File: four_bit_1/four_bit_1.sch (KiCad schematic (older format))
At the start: 1 part, among them P1 DIN_41612_128P

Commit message: Added in WHOMP, whatever it is
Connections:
- net CI05/: now also P1.67 (3C); no longer P1.65 (1C)
- net CO06: now also P1.68 (4C); no longer P1.66 (2C)
- net G01/: now also P1.69 (5C); no longer P1.67 (3C)
- net GND: no longer P1.77 (13C), P1.78 (14C)
- net L01/: now also P1.70 (6C); no longer P1.68 (4C)
- net L02/: now also P1.71 (7C); no longer P1.69 (5C)
- net L04/: now also P1.72 (8C); no longer P1.70 (6C)
- net WL01/: now also P1.73 (9C); no longer P1.71 (7C)
- net WL02/: now also P1.74 (10C); no longer P1.72 (8C)
- net WL03/: now also P1.75 (11C); no longer P1.73 (9C)
- net WL04/: now also P1.76 (12C); no longer P1.74 (10C)
- net XUY01/: now also P1.77 (13C); no longer P1.75 (11C)
- net XUY02/: now also P1.78 (14C); no longer P1.76 (12C)
- new net WHOMP: P1.65 (1C)
- new net WHOMPA: P1.66 (2C)
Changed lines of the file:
@@
 $EndDescr
 $Sheet
-S 1750 1200 1400 7250
+S 1750 1200 1400 7600
 U 5684C508
 F0 "A08_1" 60
@@
 F60 "_WL1" O R 3150 4050 60
 F61 "_WL1/" O R 3150 4150 60
-F62 "_MWL1" O R 3150 4600 60
+F62 "_MWL1" O R 3150 4750 60
 F63 "_CI_OUT" O R 3150 2750 60
 F64 "_CO_IN" I L 1750 3650 60
@@
 F96 "_WL2" O R 3150 4250 60
 F97 "_WL2/" O R 3150 4350 60
-F98 "_MWL2" O R 3150 4700 60
+F98 "_MWL2" O R 3150 4850 60
 F99 "_RL1/" O R 3150 3850 60
 F100 "_RL2/" O R 3150 3950 60
+F101 "_RL_OUT_2" O R 3150 4600 60
+F102 "_RL_OUT_1" O R 3150 4500 60
+F103 "_WHOMPA" I L 1750 8700 60
+F104 "_WHOMP_1" I L 1750 8500 60
+F105 "_WHOMP_2" I L 1750 8600 60
 $EndSheet
 $Comp
@@
 $EndComp
 $Sheet
-S 4300 1200 1400 7250
+S 4300 1200 1400 7600
 U 5689EF80
 F0 "A08_2" 60
@@
 F60 "_WL1" O R 5700 4050 60
 F61 "_WL1/" O R 5700 4150 60
-F62 "_MWL1" O R 5700 4600 60
+F62 "_MWL1" O R 5700 4750 60
 F63 "_CI_OUT" O R 5700 2750 60
 F64 "_CO_IN" I L 4300 3650 60
@@
 F96 "_WL2" O R 5700 4250 60
 F97 "_WL2/" O R 5700 4350 60
-F98 "_MWL2" O R 5700 4700 60
+F98 "_MWL2" O R 5700 4850 60
 F99 "_RL1/" O R 5700 3850 60
 F100 "_RL2/" O R 5700 3950 60
+F101 "_RL_OUT_2" O R 5700 4600 60
+F102 "_RL_OUT_1" O R 5700 4500 60
+F103 "_WHOMPA" I L 4300 8700 60
+F104 "_WHOMP_1" I L 4300 8500 60
+F105 "_WHOMP_2" I L 4300 8600 60
 $EndSheet
 Text GLabel 1650 1300 0    60   Input ~ 0
@@
 $EndComp
 Wire Wire Line
-	9700 2150 9800 2150
-Wire Wire Line
-	9700 2250 9800 2250
-Connection ~ 9700 2250
-Wire Wire Line
 	9700 2350 9800 2350
-Connection ~ 9700 2350
 Wire Wire Line
 	9700 2450 9800 2450
@@
 Text Label 5850 2000 0    60   ~ 0
 G04/
-Text GLabel 9700 1250 0    60   Input ~ 0
+Text GLabel 9700 1450 0    60   Input ~ 0
 L01/
 Wire Wire Line
-	9800 1250 9700 1250
-Text GLabel 9700 1350 0    60   Input ~ 0
+	9800 1450 9700 1450
+Text GLabel 9700 1550 0    60   Input ~ 0
 L02/
 Wire Wire Line
-	9800 1350 9700 1350
-Wire Wire Line
-	9700 2150 9700 4200
-Text GLabel 9700 1550 0    60   BiDi ~ 0
+	9800 1550 9700 1550
+Wire Wire Line
+	9700 2350 9700 4200
+Text GLabel 9700 1750 0    60   BiDi ~ 0
 WL01/
-Wire Wire Line
-	9800 1550 9700 1550
-Text GLabel 9700 1650 0    60   BiDi ~ 0
-WL02/
-Wire Wire Line
-	9800 1650 9700 1650
-Text GLabel 9700 1750 0    60   BiDi ~ 0
-WL03/
 Wire Wire Line
 	9800 1750 9700 1750
 Text GLabel 9700 1850 0    60   BiDi ~ 0
+WL02/
+Wire Wire Line
+	9800 1850 9700 1850
+Text GLabel 9700 1950 0    60   BiDi ~ 0
+WL03/
+Wire Wire Line
+	9800 1950 9700 1950
+Text GLabel 9700 2050 0    60   BiDi ~ 0
 WL04/
 Wire Wire Line
-	9800 1850 9700 1850
+	9800 2050 9700 2050
 Text GLabel 5800 2750 2    60   Output ~ 0
 CI05/
@@
 Wire Wire Line
 	5700 2850 5800 2850
-Text GLabel 9700 950  0    60   Input ~ 0
+Text GLabel 9700 1150 0    60   Input ~ 0
 CI05/
 Wire Wire Line
-	9800 950  9700 950
-Text GLabel 9700 1050 0    60   Input ~ 0
+	9800 1150 9700 1150
+Text GLabel 9700 1250 0    60   Input ~ 0
 CO06
 Wire Wire Line
-	9800 1050 9700 1050
+	9800 1250 9700 1250
 Text GLabel 5800 2200 2    60   Output ~ 0
 L04/
 Wire Wire Line
 	5700 2200 5800 2200
-Text GLabel 9700 1450 0    60   Input ~ 0
+Text GLabel 9700 1650 0    60   Input ~ 0
 L04/
 Wire Wire Line
-	9800 1450 9700 1450
+	9800 1650 9700 1650
 Wire Wire Line
 	3150 1800 3250 1800
 Text GLabel 3250 1800 2    60   Output ~ 0
 G01/
-Text GLabel 9700 1150 0    60   Input ~ 0
+Text GLabel 9700 1350 0    60   Input ~ 0
 G01/
 Wire Wire Line
-	9800 1150 9700 1150
+	9800 1350 9700 1350
 Text GLabel 3250 3350 2    60   Output ~ 0
 XUY01/
@@
 Wire Wire Line
 	3150 3450 3250 3450
-Text GLabel 9700 1950 0    60   Input ~ 0
+Text GLabel 9700 2150 0    60   Input ~ 0
 XUY01/
 Wire Wire Line
-	9800 1950 9700 1950
-Text GLabel 9700 2050 0    60   Input ~ 0
+	9800 2150 9700 2150
+Text GLabel 9700 2250 0    60   Input ~ 0
 XUY02/
 Wire Wire Line
-	9800 2050 9700 2050
+	9800 2250 9700 2250
+Text GLabel 1650 8700 0    60   Input ~ 0
+WHOMPA
+Wire Wire Line
+	1750 8700 1650 8700
+$Comp
+L GND #PWR09
+U 1 1 56BB3258
+P 3750 8800
+F 0 "#PWR09" H 3750 8550 50  0001 C CNN
+F 1 "GND" H 3750 8650 50  0000 C CNN
+F 2 "" H 3750 8800 60  0000 C CNN
+F 3 "" H 3750 8800 60  0000 C CNN
+	1    3750 8800
+	1    0    0    -1
+$EndComp
+Wire Wire Line
+	4300 8700 3750 8700
+Text GLabel 1650 8600 0    60   Input ~ 0
+WHOMP
+Wire Wire Line
+	1750 8600 1650 8600
+$Comp
+L GND #PWR010
+U 1 1 56C05747
+P 1050 8600
+F 0 "#PWR010" H 1050 8350 50  0001 C CNN
+F 1 "GND" H 1050 8450 50  0000 C CNN
+F 2 "" H 1050 8600 60  0000 C CNN
+F 3 "" H 1050 8600 60  0000 C CNN
+	1    1050 8600
+	1    0    0    -1
+$EndComp
+Wire Wire Line
+	1750 8500 1050 8500
+Wire Wire Line
+	1050 8500 1050 8600
+Connection ~ 3750 8700
+Text GLabel 4200 8600 0    60   Input ~ 0
+WHOMP
+Wire Wire Line
+	4300 8600 4200 8600
+Wire Wire Line
+	3750 8500 3750 8800
+Wire Wire Line
+	3750 8500 4300 8500
+Text GLabel 9700 950  0    60   Output ~ 0
+WHOMP
+Wire Wire Line
+	9800 950  9700 950
+Text GLabel 9700 1050 0    60   Output ~ 0
+WHOMPA
+Wire Wire Line
+	9800 1050 9700 1050
 $EndSCHEMATC

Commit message: Added and tied in module 12, parity & s register
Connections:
- net G01/: now also P1.70 (6C); no longer P1.69 (5C)
- net GND: no longer P1.79 (15C), P1.80 (16C), P1.81 (17C), P1.82 (18C)
- net L01/: now also P1.74 (10C); no longer P1.70 (6C)
- net L02/: now also P1.75 (11C); no longer P1.71 (7C)
- net L04/: now also P1.76 (12C); no longer P1.72 (8C)
- net WL01/: now also P1.77 (13C); no longer P1.73 (9C)
- net WL02/: now also P1.78 (14C); no longer P1.74 (10C)
- net WL03/: now also P1.79 (15C); no longer P1.75 (11C)
- net WL04/: now also P1.80 (16C); no longer P1.76 (12C)
- net XUY01/: now also P1.81 (17C); no longer P1.77 (13C)
- net XUY02/: now also P1.82 (18C); no longer P1.78 (14C)
- new net G01: P1.69 (5C)
- new net G02: P1.71 (7C)
- new net G03: P1.72 (8C)
- new net G04: P1.73 (9C)
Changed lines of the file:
@@
 $EndComp
 Wire Wire Line
-	9700 2350 9800 2350
-Wire Wire Line
-	9700 2450 9800 2450
-Connection ~ 9700 2450
-Wire Wire Line
-	9700 2550 9800 2550
-Connection ~ 9700 2550
-Wire Wire Line
-	9700 2650 9800 2650
-Connection ~ 9700 2650
-Wire Wire Line
 	9700 2750 9800 2750
-Connection ~ 9700 2750
 Wire Wire Line
 	9700 2850 9800 2850
@@
 Text Label 5850 2000 0    60   ~ 0
 G04/
-Text GLabel 9700 1450 0    60   Input ~ 0
+Text GLabel 9700 1850 0    60   Input ~ 0
 L01/
 Wire Wire Line
-	9800 1450 9700 1450
-Text GLabel 9700 1550 0    60   Input ~ 0
+	9800 1850 9700 1850
+Text GLabel 9700 1950 0    60   Input ~ 0
 L02/
 Wire Wire Line
-	9800 1550 9700 1550
-Wire Wire Line
-	9700 2350 9700 4200
-Text GLabel 9700 1750 0    60   BiDi ~ 0
+	9800 1950 9700 1950
+Text GLabel 9700 2150 0    60   BiDi ~ 0
 WL01/
 Wire Wire Line
-	9800 1750 9700 1750
-Text GLabel 9700 1850 0    60   BiDi ~ 0
+	9800 2150 9700 2150
+Text GLabel 9700 2250 0    60   BiDi ~ 0
 WL02/
 Wire Wire Line
-	9800 1850 9700 1850
-Text GLabel 9700 1950 0    60   BiDi ~ 0
+	9800 2250 9700 2250
+Text GLabel 9700 2350 0    60   BiDi ~ 0
 WL03/
 Wire Wire Line
-	9800 1950 9700 1950
-Text GLabel 9700 2050 0    60   BiDi ~ 0
+	9800 2350 9700 2350
+Text GLabel 9700 2450 0    60   BiDi ~ 0
 WL04/
 Wire Wire Line
-	9800 2050 9700 2050
+	9800 2450 9700 2450
 Text GLabel 5800 2750 2    60   Output ~ 0
 CI05/
@@
 Wire Wire Line
 	5700 2200 5800 2200
-Text GLabel 9700 1650 0    60   Input ~ 0
+Text GLabel 9700 2050 0    60   Input ~ 0
 L04/
 Wire Wire Line
-	9800 1650 9700 1650
+	9800 2050 9700 2050
 Wire Wire Line
 	3150 1800 3250 1800
 Text GLabel 3250 1800 2    60   Output ~ 0
 G01/
-Text GLabel 9700 1350 0    60   Input ~ 0
+Text GLabel 9700 1450 0    60   Input ~ 0
 G01/
 Wire Wire Line
-	9800 1350 9700 1350
+	9800 1450 9700 1450
 Text GLabel 3250 3350 2    60   Output ~ 0
 XUY01/
@@
 Wire Wire Line
 	3150 3450 3250 3450
-Text GLabel 9700 2150 0    60   Input ~ 0
+Text GLabel 9700 2550 0    60   Input ~ 0
 XUY01/
 Wire Wire Line
-	9800 2150 9700 2150
-Text GLabel 9700 2250 0    60   Input ~ 0
+	9800 2550 9700 2550
+Text GLabel 9700 2650 0    60   Input ~ 0
 XUY02/
 Wire Wire Line
-	9800 2250 9700 2250
+	9800 2650 9700 2650
 Text GLabel 1650 8700 0    60   Input ~ 0
 WHOMPA
@@
 Wire Wire Line
 	9800 1050 9700 1050
+Wire Wire Line
+	3150 1700 3250 1700
+Text GLabel 3250 1700 2    60   Output ~ 0
+G01
+Wire Wire Line
+	3150 1900 3250 1900
+Text GLabel 3250 1900 2    60   Output ~ 0
+G02
+Wire Wire Line
+	5700 1700 5800 1700
+Text GLabel 5800 1700 2    60   Output ~ 0
+G03
+Wire Wire Line
+	5700 1900 5800 1900
+Text GLabel 5800 1900 2    60   Output ~ 0
+G04
+Wire Wire Line
+	9700 2750 9700 4200
+Text GLabel 9700 1350 0    60   Input ~ 0
+G01
+Wire Wire Line
+	9800 1350 9700 1350
+Text GLabel 9700 1550 0    60   Input ~ 0
+G02
+Wire Wire Line
+	9800 1550 9700 1550
+Text GLabel 9700 1650 0    60   Input ~ 0
+G03
+Wire Wire Line
+	9800 1650 9700 1650
+Text GLabel 9700 1750 0    60   Input ~ 0
+G04
+Wire Wire Line
+	9800 1750 9700 1750
 $EndSCHEMATC

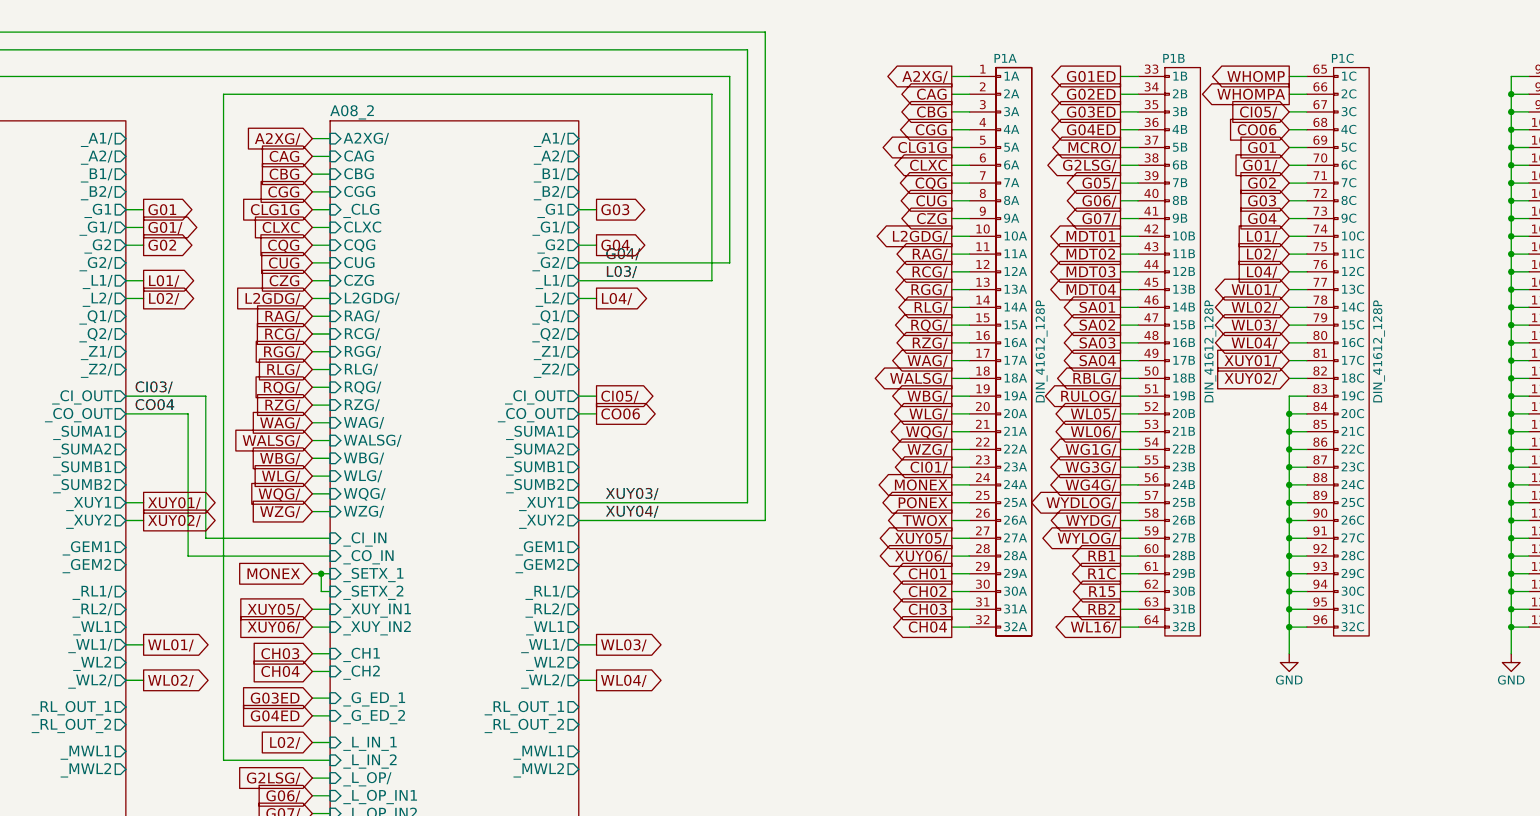
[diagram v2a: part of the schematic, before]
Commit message: Added and tied in module 15, the rupt service (and banking/rope+strand selection)
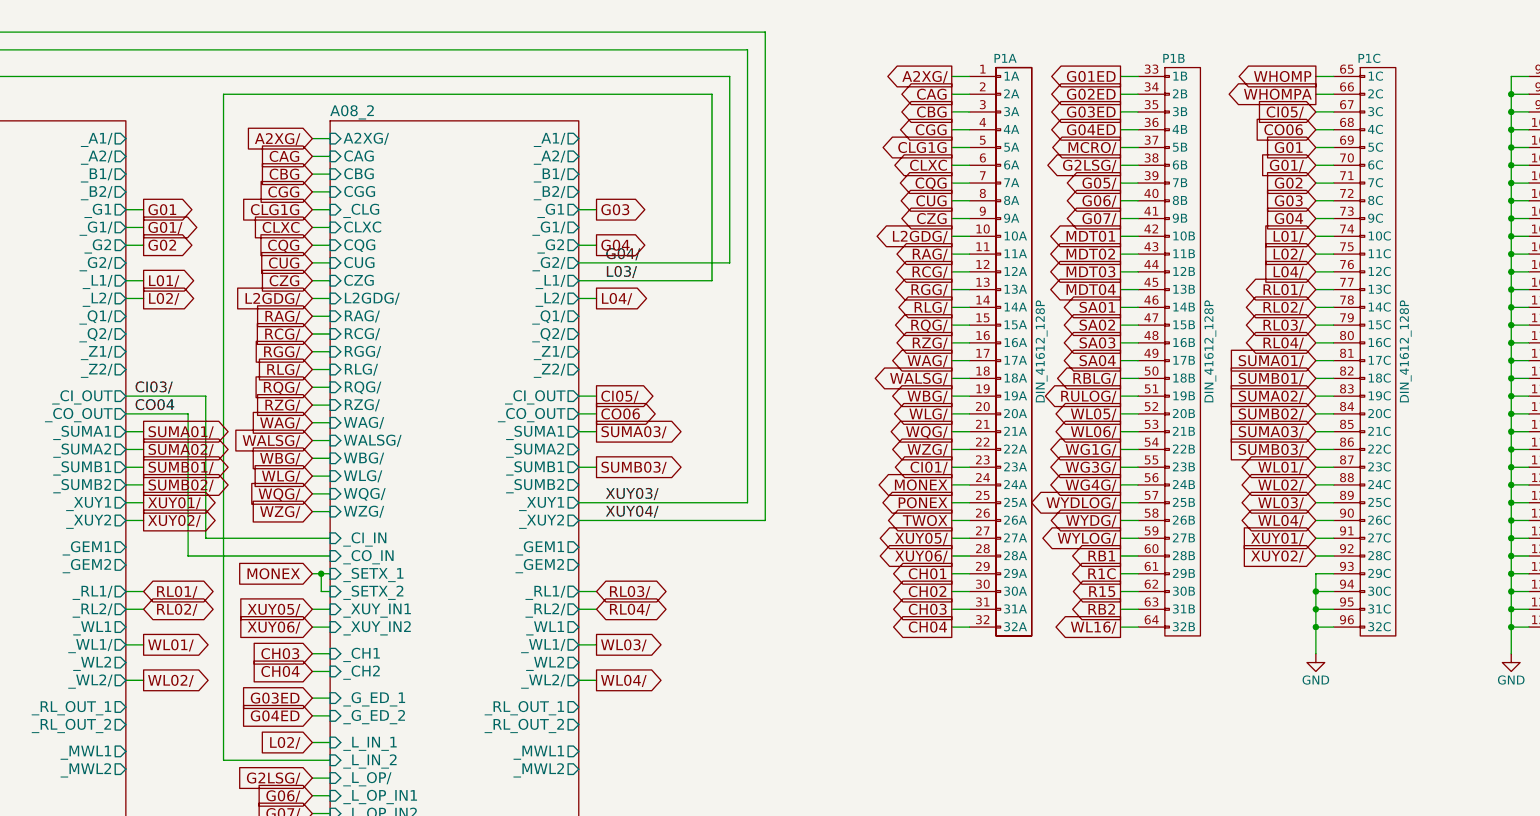
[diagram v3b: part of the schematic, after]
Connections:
- net GND: no longer P1.83 (19C), P1.84 (20C), P1.85 (21C), P1.86 (22C), P1.87 (23C), P1.88 (24C), P1.89 (25C), P1.90 (26C), P1.91 (27C), P1.92 (28C)
- net WL01/: now also P1.87 (23C); no longer P1.77 (13C)
- net WL02/: now also P1.88 (24C); no longer P1.78 (14C)
- net WL03/: now also P1.89 (25C); no longer P1.79 (15C)
- net WL04/: now also P1.90 (26C); no longer P1.80 (16C)
- net XUY01/: now also P1.91 (27C); no longer P1.81 (17C)
- net XUY02/: now also P1.92 (28C); no longer P1.82 (18C)
- new net RL01/: P1.77 (13C)
- new net RL02/: P1.78 (14C)
- new net RL03/: P1.79 (15C)
- new net RL04/: P1.80 (16C)
- new net SUMA01/: P1.81 (17C)
- new net SUMA02/: P1.83 (19C)
- new net SUMA03/: P1.85 (21C)
- new net SUMB01/: P1.82 (18C)
- new net SUMB02/: P1.84 (20C)
- new net SUMB03/: P1.86 (22C)
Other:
- moved on the sheet: P1C
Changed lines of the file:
@@
 L DIN_41612_128P P1
 U 3 1 5684CA50
-P 10000 2500
-F 0 "P1" H 10000 4150 50  0000 C CNN
-F 1 "DIN_41612_128P" V 10200 2500 50  0000 C CNN
-F 2 "" H 10000 2500 60  0000 C CNN
-F 3 "" H 10000 2500 60  0000 C CNN
-	3    10000 2500
+P 10150 2500
+F 0 "P1" H 10150 4150 50  0000 C CNN
+F 1 "DIN_41612_128P" V 10350 2500 50  0000 C CNN
+F 2 "" H 10150 2500 60  0000 C CNN
+F 3 "" H 10150 2500 60  0000 C CNN
+	3    10150 2500
 	1    0    0    -1
 $EndComp
@@
 L GND #PWR08
 U 1 1 56A4BF3C
-P 9700 4200
-F 0 "#PWR08" H 9700 3950 50  0001 C CNN
-F 1 "GND" H 9700 4050 50  0000 C CNN
-F 2 "" H 9700 4200 60  0000 C CNN
-F 3 "" H 9700 4200 60  0000 C CNN
-	1    9700 4200
+P 9850 4200
+F 0 "#PWR08" H 9850 3950 50  0001 C CNN
+F 1 "GND" H 9850 4050 50  0000 C CNN
+F 2 "" H 9850 4200 60  0000 C CNN
+F 3 "" H 9850 4200 60  0000 C CNN
+	1    9850 4200
 	1    0    0    -1
 $EndComp
 Wire Wire Line
-	9700 2750 9800 2750
-Wire Wire Line
-	9700 2850 9800 2850
-Connection ~ 9700 2850
-Wire Wire Line
-	9700 2950 9800 2950
-Connection ~ 9700 2950
-Wire Wire Line
-	9700 3050 9800 3050
-Connection ~ 9700 3050
-Wire Wire Line
-	9700 3150 9800 3150
-Connection ~ 9700 3150
-Wire Wire Line
-	9700 3250 9800 3250
-Connection ~ 9700 3250
-Wire Wire Line
-	9700 3350 9800 3350
-Connection ~ 9700 3350
-Wire Wire Line
-	9700 3450 9800 3450
-Connection ~ 9700 3450
-Wire Wire Line
-	9700 3550 9800 3550
-Connection ~ 9700 3550
-Wire Wire Line
-	9700 3650 9800 3650
-Connection ~ 9700 3650
-Wire Wire Line
-	9700 3750 9800 3750
-Connection ~ 9700 3750
-Wire Wire Line
-	9700 3850 9800 3850
-Connection ~ 9700 3850
-Wire Wire Line
-	9700 3950 9800 3950
-Connection ~ 9700 3950
-Wire Wire Line
-	9700 4050 9800 4050
-Connection ~ 9700 4050
+	9850 3750 9950 3750
+Wire Wire Line
+	9850 3850 9950 3850
+Connection ~ 9850 3850
+Wire Wire Line
+	9850 3950 9950 3950
+Connection ~ 9850 3950
+Wire Wire Line
+	9850 4050 9950 4050
+Connection ~ 9850 4050
 Wire Wire Line
 	5700 2000 6550 2000
@@
 Text Label 5850 2000 0    60   ~ 0
 G04/
-Text GLabel 9700 1850 0    60   Input ~ 0
+Text GLabel 9850 1850 0    60   Input ~ 0
 L01/
 Wire Wire Line
-	9800 1850 9700 1850
-Text GLabel 9700 1950 0    60   Input ~ 0
+	9950 1850 9850 1850
+Text GLabel 9850 1950 0    60   Input ~ 0
 L02/
 Wire Wire Line
-	9800 1950 9700 1950
-Text GLabel 9700 2150 0    60   BiDi ~ 0
+	9950 1950 9850 1950
+Text GLabel 9850 3150 0    60   BiDi ~ 0
 WL01/
 Wire Wire Line
-	9800 2150 9700 2150
-Text GLabel 9700 2250 0    60   BiDi ~ 0
+	9950 3150 9850 3150
+Text GLabel 9850 3250 0    60   BiDi ~ 0
 WL02/
 Wire Wire Line
-	9800 2250 9700 2250
-Text GLabel 9700 2350 0    60   BiDi ~ 0
+	9950 3250 9850 3250
+Text GLabel 9850 3350 0    60   BiDi ~ 0
 WL03/
 Wire Wire Line
-	9800 2350 9700 2350
-Text GLabel 9700 2450 0    60   BiDi ~ 0
+	9950 3350 9850 3350
+Text GLabel 9850 3450 0    60   BiDi ~ 0
 WL04/
 Wire Wire Line
-	9800 2450 9700 2450
+	9950 3450 9850 3450
 Text GLabel 5800 2750 2    60   Output ~ 0
 CI05/
@@
 Wire Wire Line
 	5700 2850 5800 2850
-Text GLabel 9700 1150 0    60   Input ~ 0
+Text GLabel 9850 1150 0    60   Input ~ 0
 CI05/
 Wire Wire Line
-	9800 1150 9700 1150
-Text GLabel 9700 1250 0    60   Input ~ 0
+	9950 1150 9850 1150
+Text GLabel 9850 1250 0    60   Input ~ 0
 CO06
 Wire Wire Line
-	9800 1250 9700 1250
+	9950 1250 9850 1250
 Text GLabel 5800 2200 2    60   Output ~ 0
 L04/
 Wire Wire Line
 	5700 2200 5800 2200
-Text GLabel 9700 2050 0    60   Input ~ 0
+Text GLabel 9850 2050 0    60   Input ~ 0
 L04/
 Wire Wire Line
-	9800 2050 9700 2050
+	9950 2050 9850 2050
 Wire Wire Line
 	3150 1800 3250 1800
 Text GLabel 3250 1800 2    60   Output ~ 0
 G01/
-Text GLabel 9700 1450 0    60   Input ~ 0
+Text GLabel 9850 1450 0    60   Input ~ 0
 G01/
 Wire Wire Line
-	9800 1450 9700 1450
+	9950 1450 9850 1450
 Text GLabel 3250 3350 2    60   Output ~ 0
 XUY01/
@@
 Wire Wire Line
 	3150 3450 3250 3450
-Text GLabel 9700 2550 0    60   Input ~ 0
+Text GLabel 9850 3550 0    60   Input ~ 0
 XUY01/
 Wire Wire Line
-	9800 2550 9700 2550
-Text GLabel 9700 2650 0    60   Input ~ 0
+	9950 3550 9850 3550
+Text GLabel 9850 3650 0    60   Input ~ 0
 XUY02/
 Wire Wire Line
-	9800 2650 9700 2650
+	9950 3650 9850 3650
 Text GLabel 1650 8700 0    60   Input ~ 0
 WHOMPA
@@
 Wire Wire Line
 	3750 8500 4300 8500
-Text GLabel 9700 950  0    60   Output ~ 0
+Text GLabel 9850 950  0    60   Output ~ 0
 WHOMP
 Wire Wire Line
-	9800 950  9700 950
-Text GLabel 9700 1050 0    60   Output ~ 0
+	9950 950  9850 950
+Text GLabel 9850 1050 0    60   Output ~ 0
 WHOMPA
 Wire Wire Line
-	9800 1050 9700 1050
+	9950 1050 9850 1050
 Wire Wire Line
 	3150 1700 3250 1700
@@
 Text GLabel 5800 1900 2    60   Output ~ 0
 G04
-Wire Wire Line
-	9700 2750 9700 4200
-Text GLabel 9700 1350 0    60   Input ~ 0
+Text GLabel 9850 1350 0    60   Input ~ 0
 G01
 Wire Wire Line
-	9800 1350 9700 1350
-Text GLabel 9700 1550 0    60   Input ~ 0
+	9950 1350 9850 1350
+Text GLabel 9850 1550 0    60   Input ~ 0
 G02
 Wire Wire Line
-	9800 1550 9700 1550
-Text GLabel 9700 1650 0    60   Input ~ 0
+	9950 1550 9850 1550
+Text GLabel 9850 1650 0    60   Input ~ 0
 G03
 Wire Wire Line
-	9800 1650 9700 1650
-Text GLabel 9700 1750 0    60   Input ~ 0
+	9950 1650 9850 1650
+Text GLabel 9850 1750 0    60   Input ~ 0
 G04
 Wire Wire Line
-	9800 1750 9700 1750
+	9950 1750 9850 1750
+Text GLabel 3250 2950 2    60   Output ~ 0
+SUMA01/
+Wire Wire Line
+	3150 2950 3250 2950
+Text GLabel 3250 3050 2    60   Output ~ 0
+SUMA02/
+Wire Wire Line
+	3150 3050 3250 3050
+Text GLabel 3250 3150 2    60   Output ~ 0
+SUMB01/
+Wire Wire Line
+	3150 3150 3250 3150
+Text GLabel 3250 3250 2    60   Output ~ 0
+SUMB02/
+Wire Wire Line
+	3150 3250 3250 3250
+Text GLabel 9850 2550 0    60   Input ~ 0
+SUMA01/
+Wire Wire Line
+	9950 2550 9850 2550
+Text GLabel 9850 2750 0    60   Input ~ 0
+SUMA02/
+Wire Wire Line
+	9950 2750 9850 2750
+Text GLabel 9850 2650 0    60   Input ~ 0
+SUMB01/
+Wire Wire Line
+	9950 2650 9850 2650
+Text GLabel 9850 2850 0    60   Input ~ 0
+SUMB02/
+Wire Wire Line
+	9950 2850 9850 2850
+Text GLabel 5800 2950 2    60   Output ~ 0
+SUMA03/
+Wire Wire Line
+	5700 2950 5800 2950
+Text GLabel 5800 3150 2    60   Output ~ 0
+SUMB03/
+Wire Wire Line
+	5700 3150 5800 3150
+Text GLabel 9850 2950 0    60   Input ~ 0
+SUMA03/
+Wire Wire Line
+	9950 2950 9850 2950
+Text GLabel 9850 3050 0    60   Input ~ 0
+SUMB03/
+Wire Wire Line
+	9950 3050 9850 3050
+Text GLabel 3250 3850 2    60   BiDi ~ 0
+RL01/
+Wire Wire Line
+	3150 3850 3250 3850
+Text GLabel 3250 3950 2    60   BiDi ~ 0
+RL02/
+Wire Wire Line
+	3150 3950 3250 3950
+Text GLabel 5800 3850 2    60   BiDi ~ 0
+RL03/
+Wire Wire Line
+	5700 3850 5800 3850
+Text GLabel 5800 3950 2    60   BiDi ~ 0
+RL04/
+Wire Wire Line
+	5700 3950 5800 3950
+Wire Wire Line
+	9850 3750 9850 4200
+Text GLabel 9850 2150 0    60   BiDi ~ 0
+RL01/
+Wire Wire Line
+	9950 2150 9850 2150
+Text GLabel 9850 2250 0    60   BiDi ~ 0
+RL02/
+Wire Wire Line
+	9950 2250 9850 2250
+Text GLabel 9850 2350 0    60   BiDi ~ 0
+RL03/
+Wire Wire Line
+	9950 2350 9850 2350
+Text GLabel 9850 2450 0    60   BiDi ~ 0
+RL04/
+Wire Wire Line
+	9950 2450 9850 2450
 $EndSCHEMATC
